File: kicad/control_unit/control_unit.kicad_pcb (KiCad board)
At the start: 2 copper layers, 50 parts

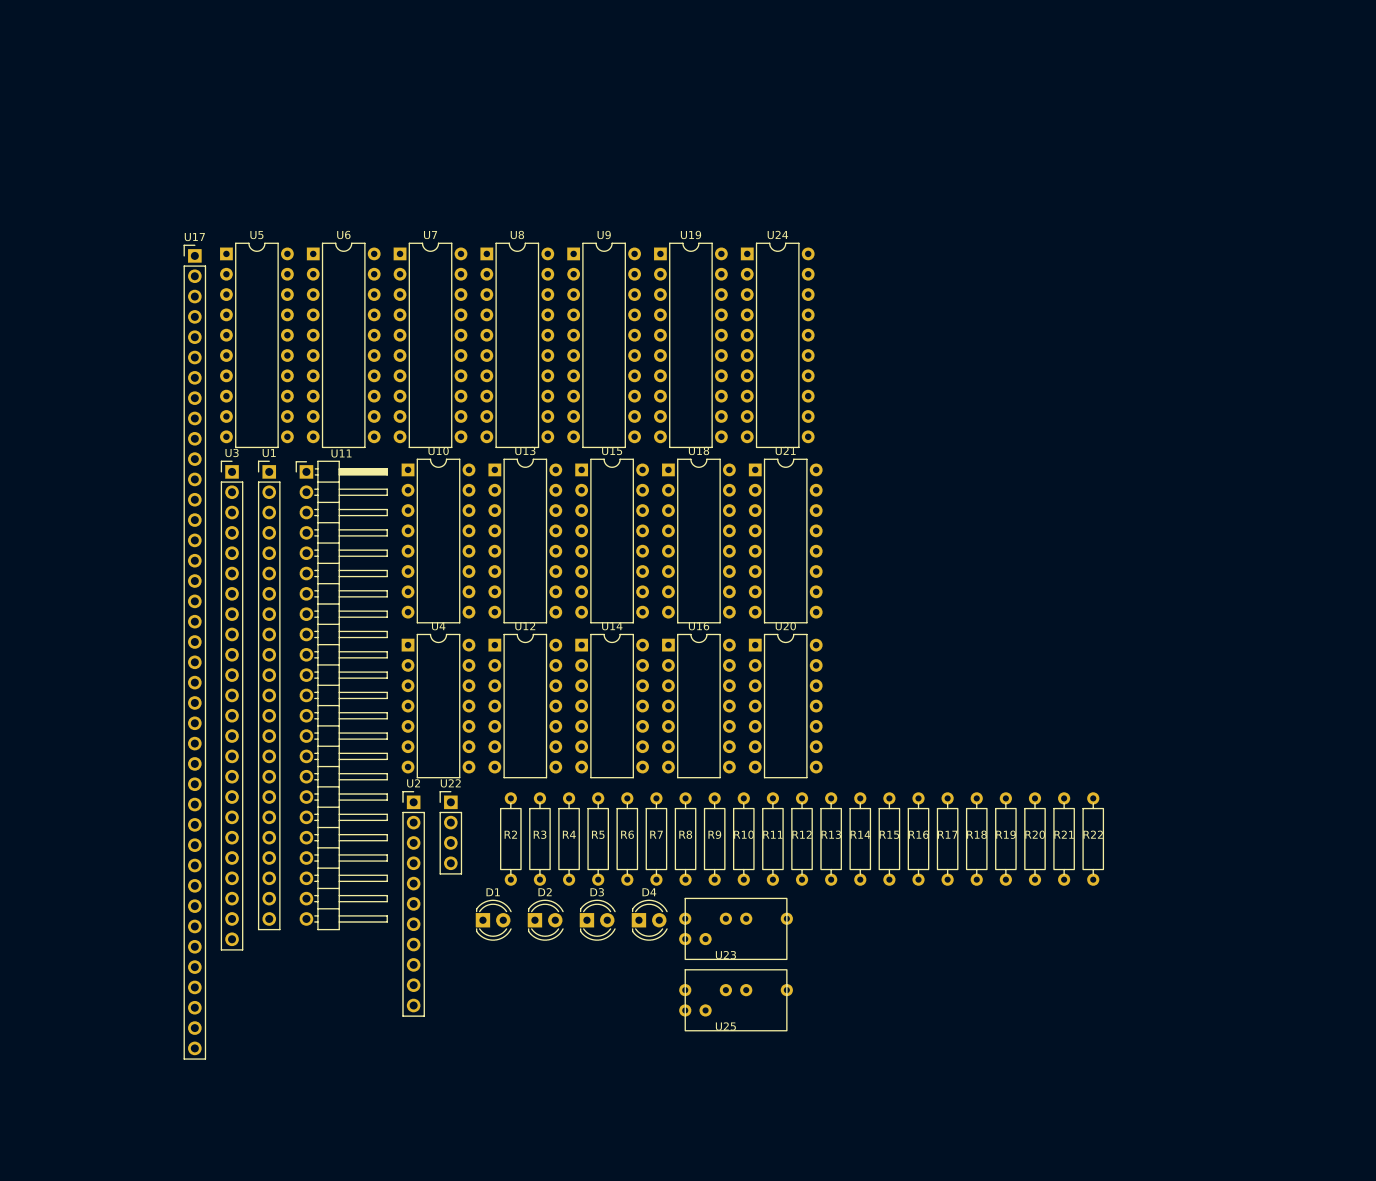
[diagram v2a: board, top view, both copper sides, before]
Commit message: Finished call stack schematic
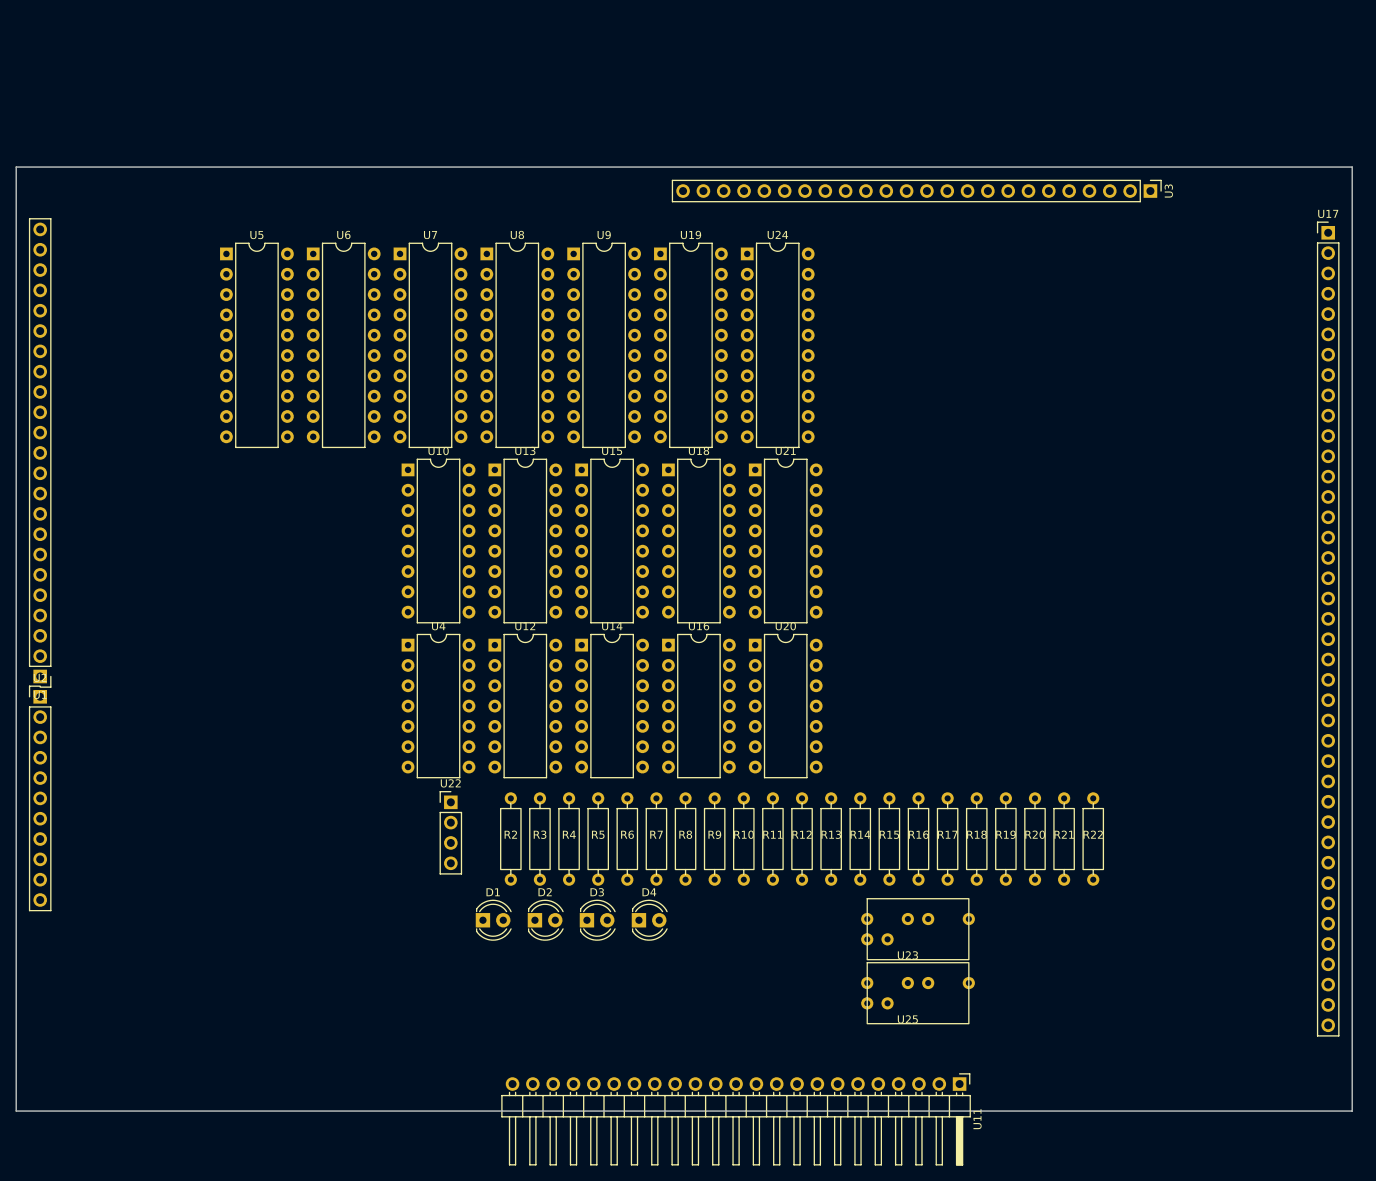
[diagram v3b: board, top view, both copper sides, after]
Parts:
- moved U17 141.7 mm to (244.0, 51.2)
- moved U3 120.0 mm to (221.8, 46.0), turned to -90 degrees
- moved U11 111.9 mm to (197.9, 157.6), turned to -90 degrees
- moved U2 48.5 mm to (83.0, 109.2)
- moved U1 38.4 mm to (83.0, 106.7), turned to 180 degrees
- moved U25 22.8 mm to (191.5, 150.1)
- moved U23 22.7 mm to (191.5, 142.1)
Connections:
- U15 pad 11: Net-(U15-B0) -> Net-(D1-K)
- U15 pad 15: Net-(U15-B0) -> Net-(D1-K)
- U15 pad 2: Net-(U15-B0) -> Net-(D1-K)
- U15 pad 6: Net-(U15-B0) -> Net-(D1-K)
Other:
- board outline added: 167 x 118 mm

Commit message: Finished prog memory timing diagrams
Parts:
- U17: footprint Connector_PinHeader_2.54mm:PinHeader_1x40_P2.54mm_Vertical -> Connector_PinHeader_2.54mm:PinHeader_1x39_P2.54mm_Vertical
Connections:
- U17 pad 4: Net-(D1-K) -> Net-(U1-V+)
- U17 pad 7: Net-(U1-V+) -> unconnected-(U17-NC-Pad7)
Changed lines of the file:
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@@
 	(net 130 "Net-(U21-Σ1)")
 	(net 131 "Net-(U17-Done)")
+	(net 132 "unconnected-(U17-NC-Pad7)")
 	(footprint "LED_THT:LED_D4.0mm"
 		(layer "F.Cu")
@@
 		)
 	)
-	(footprint "Connector_PinHeader_2.54mm:PinHeader_1x40_P2.54mm_Vertical"
+	(footprint "Connector_PinHeader_2.54mm:PinHeader_1x39_P2.54mm_Vertical"
 		(layer "F.Cu")
 		(at 244 51.22)
-		(descr "Through hole straight pin header, 1x40, 2.54mm pitch, single row")
-		(tags "Through hole pin header THT 1x40 2.54mm single row")
+		(descr "Through hole straight pin header, 1x39, 2.54mm pitch, single row")
+		(tags "Through hole pin header THT 1x39 2.54mm single row")
 		(property "Reference" "U17"
 			(at 0 -2.33 0)
@@
 		)
 		(property "Value" "~"
-			(at 0 101.39 0)
+			(at 0 98.85 0)
 			(layer "F.Fab")
 			(effects
@@
 			)
 		)
-		(property "Footprint" "Connector_PinHeader_2.54mm:PinHeader_1x40_P2.54mm_Vertical"
+		(property "Footprint" "Connector_PinHeader_2.54mm:PinHeader_1x39_P2.54mm_Vertical"
 			(at 0 0 0)
 			(unlocked yes)
@@
 		(fp_line
 			(start -1.33 1.27)
-			(end -1.33 100.39)
+			(end -1.33 97.85)
 			(stroke
 				(width 0.12)
@@
 		)
 		(fp_line
-			(start -1.33 100.39)
-			(end 1.33 100.39)
+			(start -1.33 97.85)
+			(end 1.33 97.85)
 			(stroke
 				(width 0.12)
@@
 		(fp_line
 			(start 1.33 1.27)
-			(end 1.33 100.39)
+			(end 1.33 97.85)
 			(stroke
 				(width 0.12)
@@
 		(fp_line
 			(start -1.8 -1.8)
-			(end -1.8 100.85)
+			(end -1.8 98.3)
 			(stroke
 				(width 0.05)
@@
 		)
 		(fp_line
-			(start -1.8 100.85)
-			(end 1.8 100.85)
+			(start -1.8 98.3)
+			(end 1.8 98.3)
 			(stroke
 				(width 0.05)
@@
 		)
 		(fp_line
-			(start 1.8 100.85)
+			(start 1.8 98.3)
 			(end 1.8 -1.8)
 			(stroke
@@
 		)
 		(fp_line
-			(start -1.27 100.33)
+			(start -1.27 97.79)
 			(end -1.27 -0.635)
 			(stroke
@@
 		(fp_line
 			(start 1.27 -1.27)
-			(end 1.27 100.33)
+			(end 1.27 97.79)
 			(stroke
 				(width 0.1)
@@
 		)
 		(fp_line
-			(start 1.27 100.33)
-			(end -1.27 100.33)
+			(start 1.27 97.79)
+			(end -1.27 97.79)
 			(stroke
 				(width 0.1)
@@
 		)
 		(fp_text user "${REFERENCE}"
-			(at 0 49.53 90)
+			(at 0 48.26 90)
 			(layer "F.Fab")
 			(effects
@@
 			(layers "*.Cu" "*.Mask")
 			(remove_unused_layers no)
-			(net 15 "Net-(D1-K)")
-			(pinfunction "W/R#_select")
+			(net 14 "Net-(U1-V+)")
+			(pinfunction "Read_enable")
 			(pintype "bidirectional")
 		)
@@
 			(remove_unused_layers no)
 			(net 90 "Net-(U11-PROG_READ)")
-			(pinfunction "Start")
+			(pinfunction "Read")
 			(pintype "bidirectional")
 		)
@@
 			(layers "*.Cu" "*.Mask")
 			(remove_unused_layers no)
-			(net 14 "Net-(U1-V+)")
-			(pinfunction "OE")
-			(pintype "bidirectional")
+			(net 132 "unconnected-(U17-NC-Pad7)")
+			(pinfunction "NC")
+			(pintype "no_connect")
 		)
 		(pad "8" thru_hole oval
@@
 			(pintype "bidirectional")
 		)
-		(pad "40" thru_hole oval
-			(at 0 99.06)
-			(size 1.7 1.7)
-			(drill 1)
-			(layers "*.Cu" "*.Mask")
-			(remove_unused_layers no)
-			(net 2 "Net-(U1-ENABLE)")
-			(pinfunction "ENABLE")
-			(pintype "bidirectional")
-		)
-		(model "${KICAD8_3DMODEL_DIR}/Connector_PinHeader_2.54mm.3dshapes/PinHeader_1x40_P2.54mm_Vertical.wrl"
+		(model "${KICAD8_3DMODEL_DIR}/Connector_PinHeader_2.54mm.3dshapes/PinHeader_1x39_P2.54mm_Vertical.wrl"
 			(offset
 				(xyz 0 0 0)
@@
 		)
 		(fp_text user "${REFERENCE}"
-			(at 0 27.94 270)
+			(at 0 27.94 -90)
 			(layer "F.Fab")
 			(effects

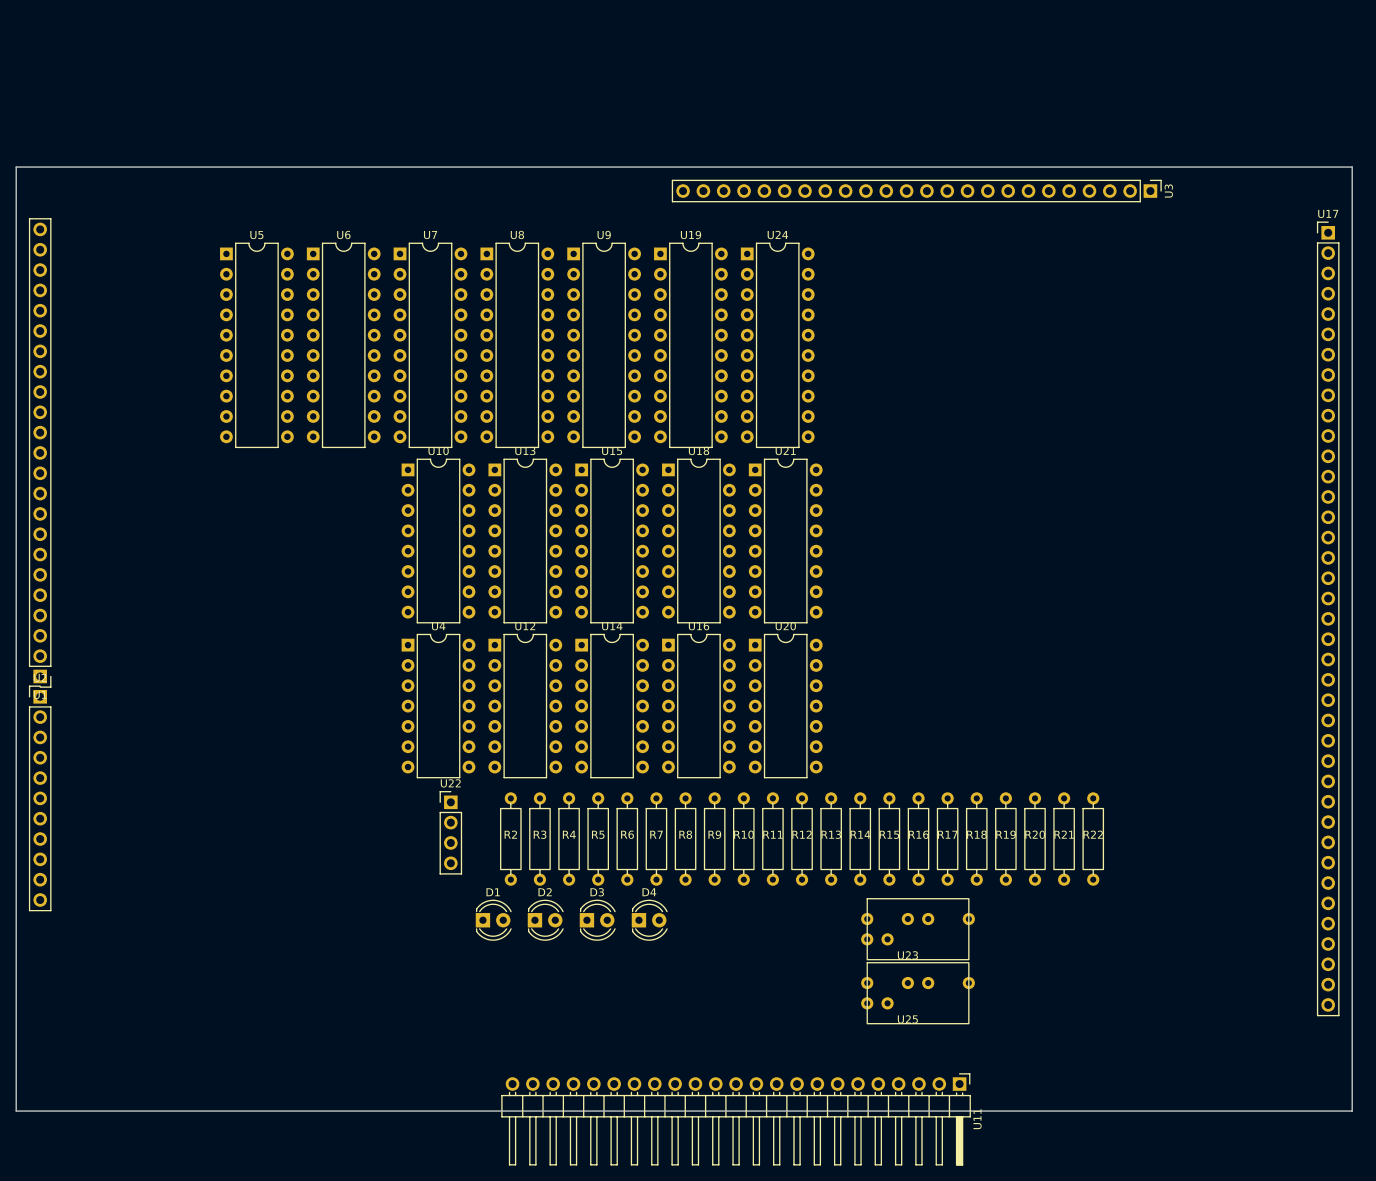
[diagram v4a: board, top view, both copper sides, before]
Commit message: Finished some more PCBs and uploaded to JLCPCB
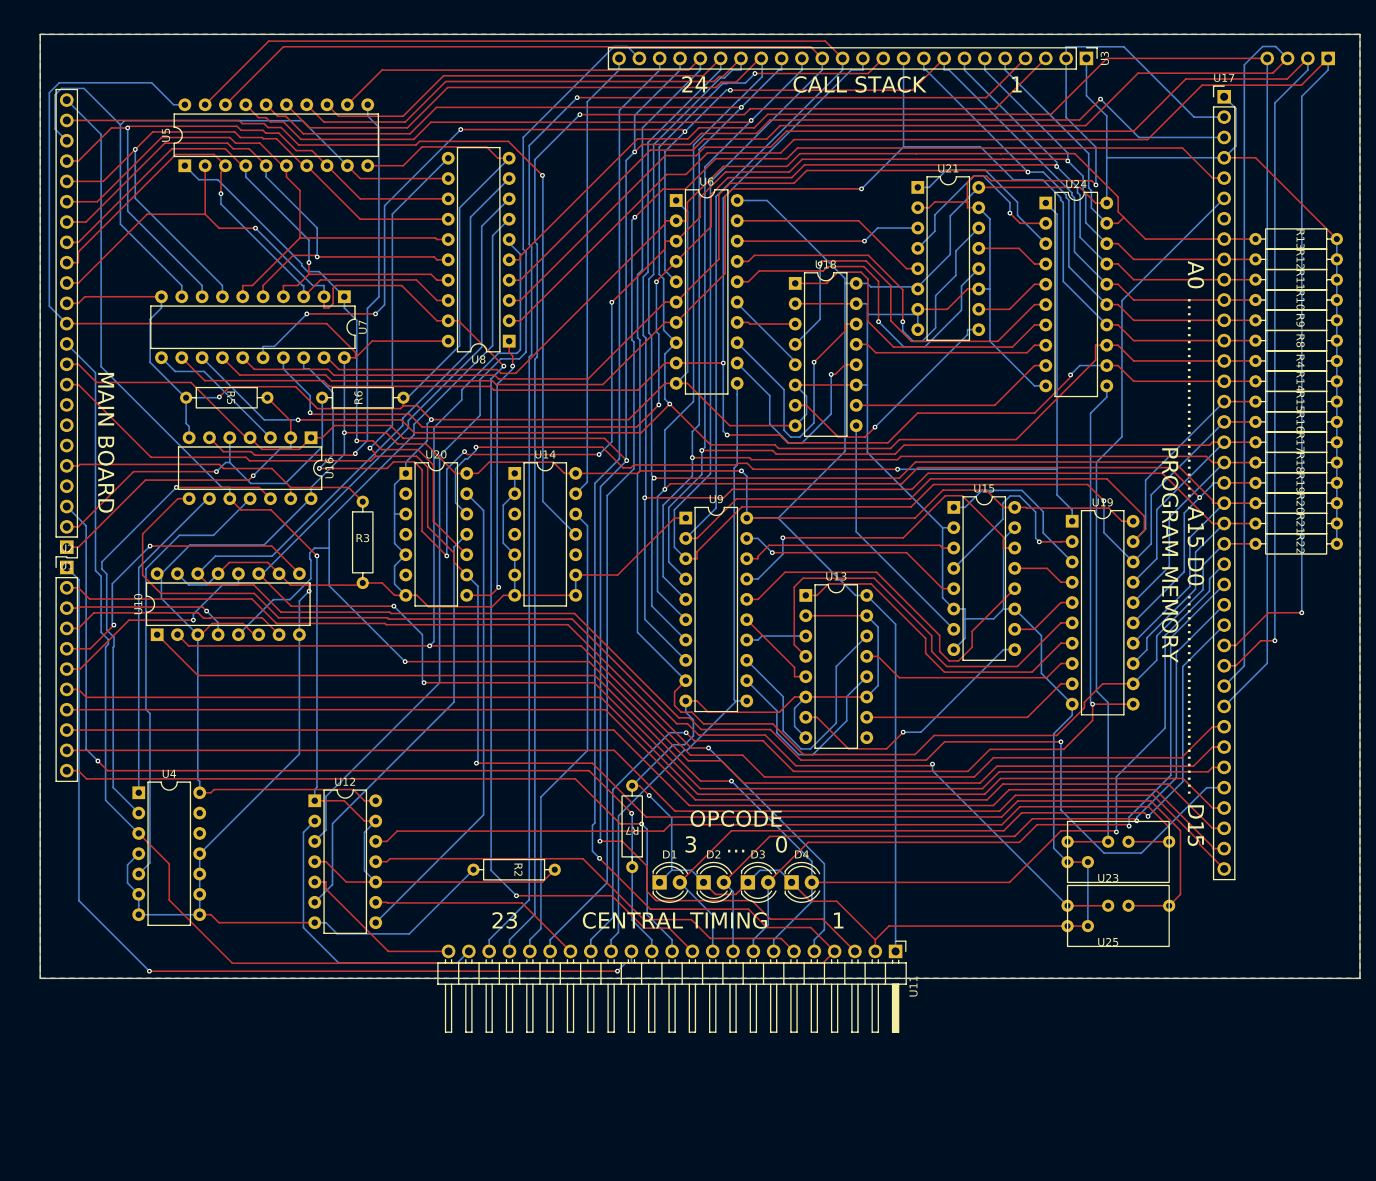
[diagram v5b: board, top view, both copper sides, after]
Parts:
- U22: moved to B.Cu
- moved U22 143.8 mm to (244.0, 29.4), turned to 90 degrees
- moved R4 108.8 mm to (240.0, 67.2), turned to -90 degrees
- moved R8 98.5 mm to (240.0, 64.7), turned to -90 degrees
- moved R9 97.4 mm to (240.0, 62.2), turned to -90 degrees
- moved R10 96.5 mm to (240.0, 59.6), turned to -90 degrees
- moved R11 95.7 mm to (240.0, 57.1), turned to -90 degrees
- moved R12 95.2 mm to (240.0, 54.5), turned to -90 degrees
- moved R13 94.9 mm to (240.0, 52.0), turned to -90 degrees
- moved R14 79.0 mm to (240.0, 69.8), turned to -90 degrees
- moved R15 74.7 mm to (240.0, 72.3), turned to -90 degrees
- moved R5 72.1 mm to (106.3, 71.8), turned to -90 degrees
- moved R16 70.3 mm to (240.0, 74.9), turned to -90 degrees
- moved R17 66.0 mm to (240.0, 77.4), turned to -90 degrees
- moved R6 64.3 mm to (123.3, 71.8), turned to 90 degrees
- moved R18 61.7 mm to (240.0, 79.9), turned to -90 degrees
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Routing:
- net Net-(D1-K): track 0.00 -> 809.4 mm, vias 0 -> 5
- net Net-(U1-V+): track 0.00 -> 571.3 mm, vias 0 -> 2
- net Net-(U1-CLK_B): track 0.00 -> 300.2 mm, vias 0 -> 1
- net Net-(U1-CLK_A): track 0.00 -> 297.4 mm, vias 0 -> 4
- net Net-(U17-A8): track 0.00 -> 244.2 mm
- net Net-(U17-A9): track 0.00 -> 241.7 mm, vias 0 -> 1
- net Net-(U17-A13): track 0.00 -> 239.6 mm, vias 0 -> 1
- net Net-(U1-READ_READY): track 0.00 -> 239.4 mm, vias 0 -> 2
- net Net-(U17-A12): track 0.00 -> 237.8 mm, vias 0 -> 2
- net Net-(U17-A14): track 0.00 -> 236.8 mm, vias 0 -> 1
- net Net-(U17-A10): track 0.00 -> 231.1 mm, vias 0 -> 2
- net Net-(U17-A11): track 0.00 -> 230.6 mm, vias 0 -> 2
- net Net-(U17-A15): track 0.00 -> 224.1 mm
- net Net-(U10-A3): track 0.00 -> 222.7 mm, vias 0 -> 1
- net Net-(U17-A6): track 0.00 -> 213.0 mm, vias 0 -> 3
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- added copper zone on B.Cu, net Net-(D1-K)
- added copper zone on F.Cu, net Net-(U1-V+)
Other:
- board size 167 x 118 mm -> 165 x 118 mm
- board text added: "0 .. 3 ALU OPCODE"
- board text added: "23 CENTRAL TIMING 1"
- board text added: "24 CALL STACK 1"
- board text added: "A0 ............................. A15 D0 ............................. D15 PROGRAM MEMORY"
- board text added: "MAIN BOARD"
- board text added: "OPCODE 3 ... 0"
